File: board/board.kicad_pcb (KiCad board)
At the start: 2 copper layers, 92 x 75.8 mm, 69 parts, among them J2 Conn_01x01, J3 Conn_01x01, J3 Conn_01x25_Socket, J4 Conn_01x01, J4 Conn_01x25_Socket, J5 Conn_01x01, J5 PJ-320B, J6 Screw_Terminal_01x02, J7 Screw_Terminal_01x02, J8 Screw_Terminal_01x02

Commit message: add РПЗ template
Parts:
- removed H1: MountingHole, MountingHole:MountingHole_3.2mm_M3
- moved G*** 38.5 mm to (126.8, 101.4)
- moved J6 23.7 mm to (186.4, 86.2)
- moved J7 23.0 mm to (186.4, 94.5)
- moved J8 22.5 mm to (186.4, 103.0)
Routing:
- net PWM2: track 0.00 -> 51.4 mm
- net NOISE_CS: track 0.00 -> 27.4 mm, vias 0 -> 2
- net NOISE_DI: track 0.00 -> 25.4 mm
- net Analog_data: track 10.9 -> 34.7 mm
- net MUX_SEL_3: track 0.00 -> 23.6 mm
- net MUX_SEL_1: track 0.00 -> 20.9 mm
- net MUX_SEL_2: track 0.00 -> 20.7 mm
- net CS_AD9833_2: track 0.00 -> 19.2 mm
- net PWM4: track 0.00 -> 18.7 mm
- net NOISE_CLK_SEL: track 0.00 -> 18.1 mm
- net MUX_SEL_4: track 0.00 -> 16.8 mm
- net NOISE_CLK: track 0.00 -> 14.9 mm

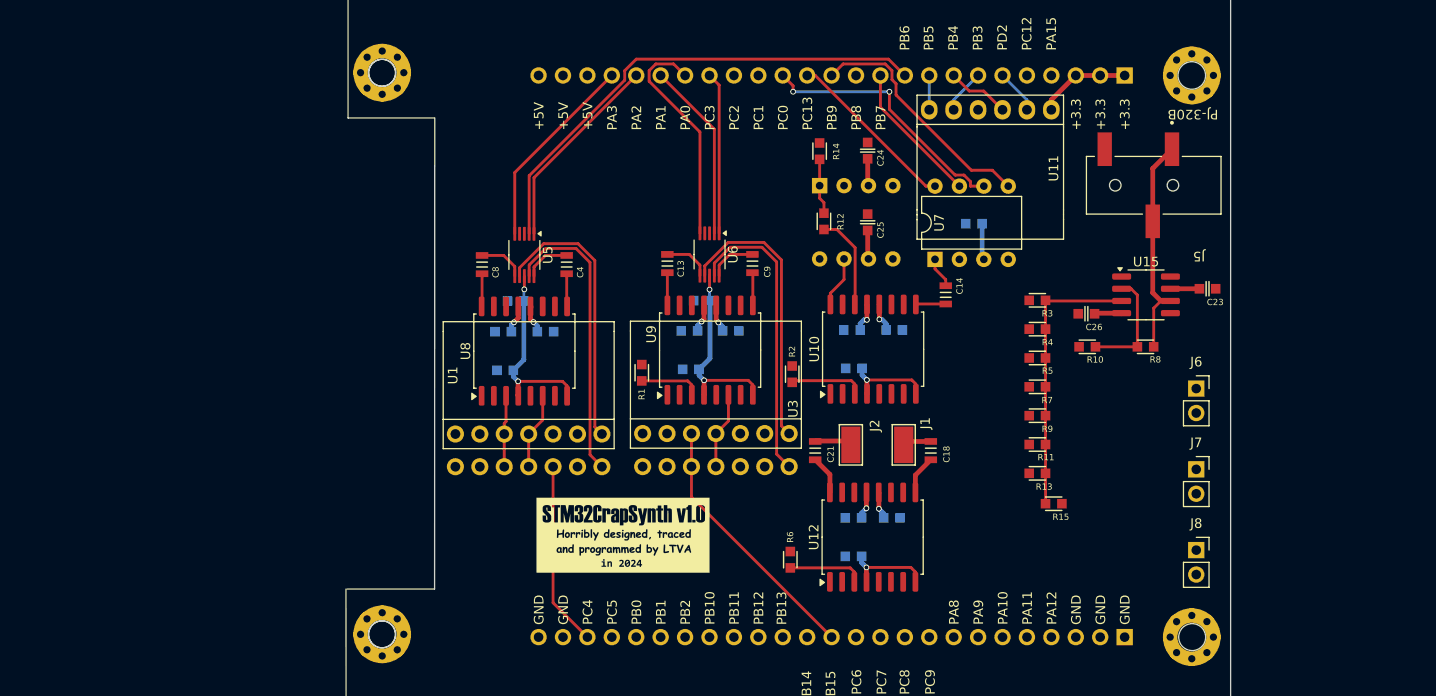
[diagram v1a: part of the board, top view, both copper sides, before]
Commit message: added DMA init
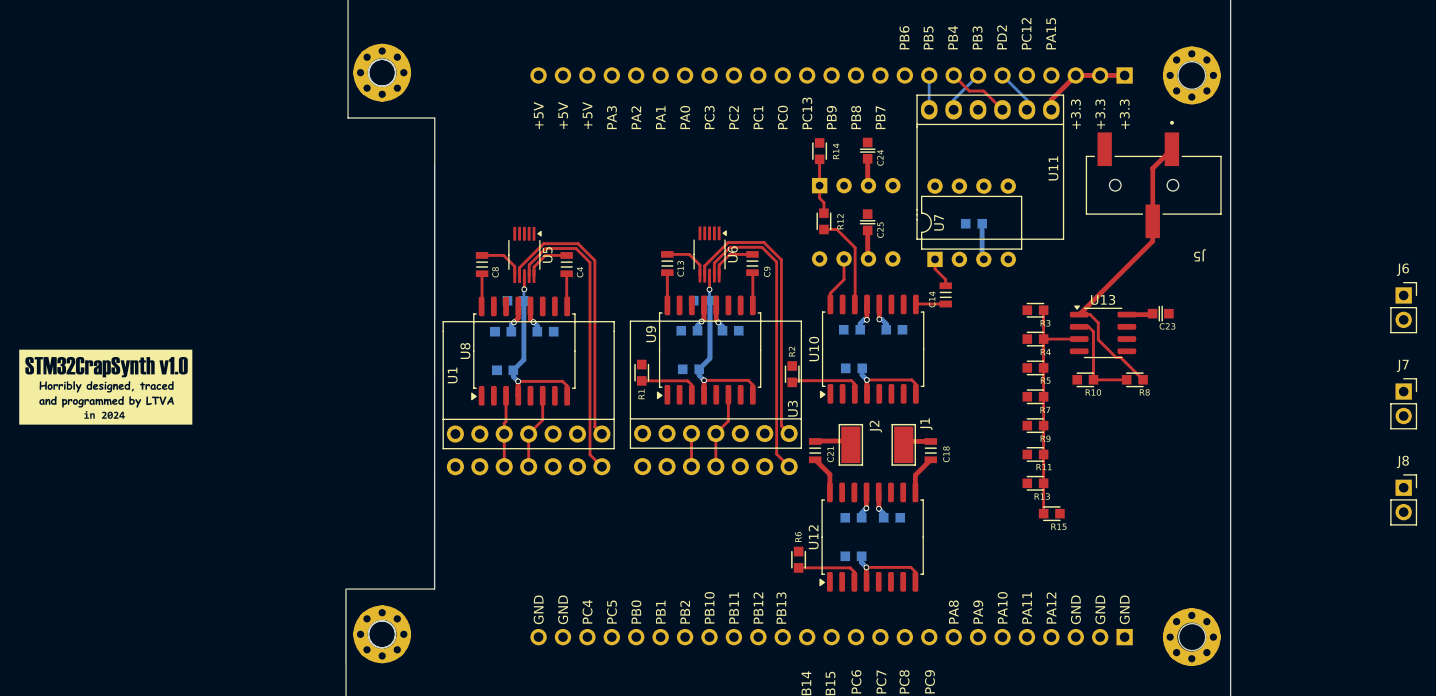
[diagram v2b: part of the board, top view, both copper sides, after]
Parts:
- removed C26: 0.22uF_0603_25V, 4ms_Capacitor:C_0603
- removed U15: ~, Package_SO:SOP-8_3.76x4.96mm_P1.27mm
- added U13: ~, Package_SO:SOIC-8_3.9x4.9mm_P1.27mm, F.Cu at (176.7, 80.4)
- moved G*** 56.0 mm to (73.0, 86.0)
- moved J6 23.7 mm to (208.0, 76.5)
- moved J7 23.0 mm to (208.0, 86.5)
- moved J8 22.5 mm to (208.0, 96.5)
- moved C23 5.52 mm to (182.7, 78.4)
- moved R8 3.61 mm to (180.0, 85.2)
- moved R10 3.44 mm to (174.9, 85.2)
- moved R11 1.05 mm to (169.7, 93.0)
- moved R13 1.05 mm to (169.7, 96.0)
- moved R3 1.05 mm to (169.7, 78.0)
- moved R4 1.05 mm to (169.7, 81.0)
- moved R5 1.05 mm to (169.7, 84.0)
- moved R7 1.05 mm to (169.7, 87.0)
- moved R9 1.05 mm to (169.7, 90.0)
- moved R15 1.05 mm to (171.4, 99.2)
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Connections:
- C23 pad 1: P,+15 -> +5V
- J3 pad 11: /PC7 -> ZCEN_2
- J3 pad 12: ATTEN_CS -> ZCEN_1
- J3 pad 14: ZCEN_DAC -> /PB14/adc4_in4
- J3 pad 16: ZCEN_2 -> /PB12/adc4_in3
- J3 pad 17: CS_AD9833_4 -> /PB11
- J3 pad 18: CS_AD9833_3 -> /PB10
- J3 pad 19: ZCEN_1 -> /PB2
- J3 pad 22: CS_AD9833_1 -> /PC5/adc2_in11
- J3 pad 23: CS_AD9833_2 -> /PC4/adc2_in5
- J3 pad 6: /PA10 -> CS_AD9833_3
- J3 pad 7: /PA9 -> CS_AD9833_2
- J3 pad 9: /PC9 -> ZCEN_DAC
- J4 pad 14: NOISE_CLK_SEL -> MUX_SEL_3
- J4 pad 15: NOISE_CS -> MUX_SEL_4
- J4 pad 16: /PC1 -> NOISE_CLK_SEL
- J4 pad 18: MUX_SEL_4 -> MUX_SEL_1
- J4 pad 19: MUX_SEL_3 -> MUX_SEL_2
- J4 pad 21: MUX_SEL_1 -> ATTEN_CS
- J4 pad 22: MUX_SEL_2 -> CS_AD9833_1
- J4 pad 4: /PA15 -> NOISE_CS
- J4 pad 5: /PC12 -> CS_AD9833_4
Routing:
- net PWM2: track 51.4 -> 0.00 mm
- net NOISE_CS: track 27.4 -> 0.00 mm, vias 2 -> 0
- net NOISE_DI: track 25.4 -> 0.00 mm
- net Analog_data: track 34.7 -> 10.9 mm
- net MUX_SEL_3: track 23.6 -> 0.00 mm
- net MUX_SEL_1: track 20.9 -> 0.00 mm
- net MUX_SEL_2: track 20.7 -> 0.00 mm
- net CS_AD9833_2: track 19.2 -> 0.00 mm
- net PWM4: track 18.7 -> 0.00 mm
- net NOISE_CLK_SEL: track 18.1 -> 0.00 mm
- net MUX_SEL_4: track 16.8 -> 0.00 mm
- net NOISE_CLK: track 14.9 -> 0.00 mm
- net Net-(U13-OUT_A): track 23.0 -> 31.7 mm
- net Net-(U13-IN_A): track 29.1 -> 24.9 mm
- net P,+15: track 14.9 -> 11.9 mm
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
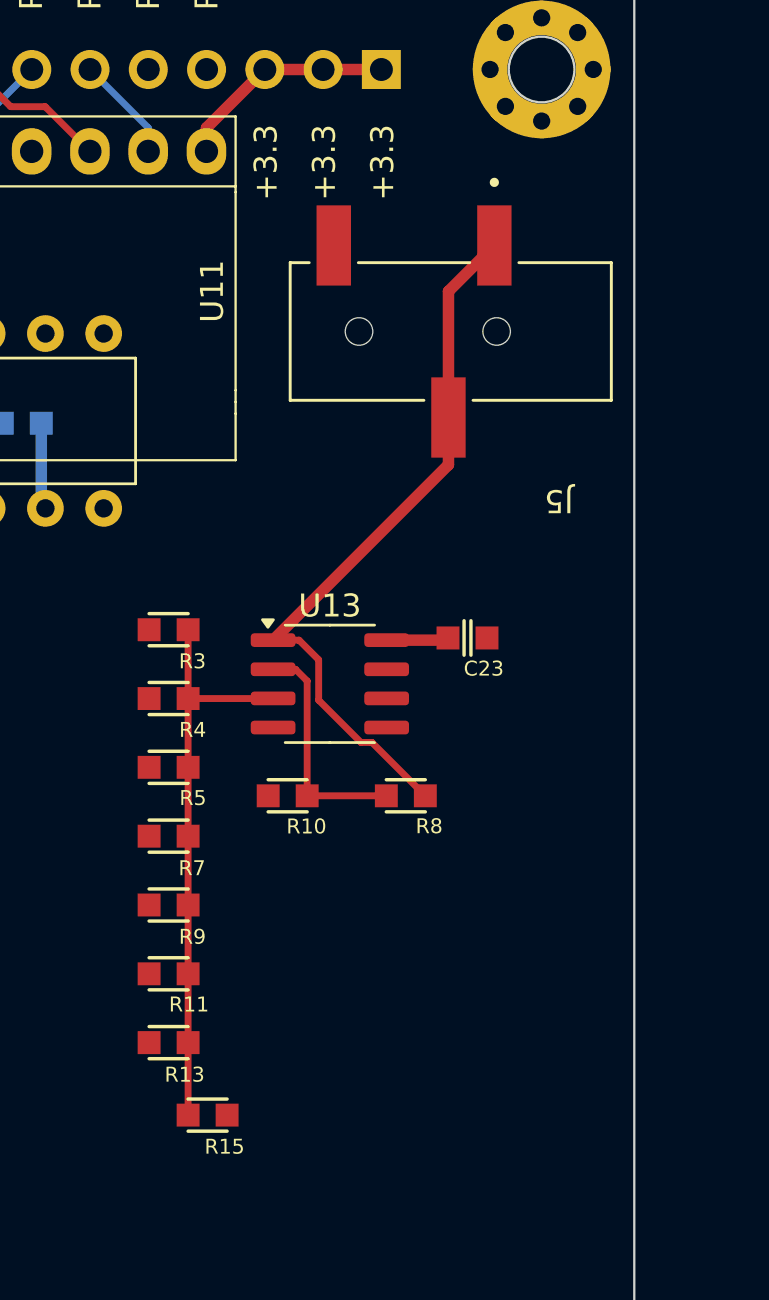
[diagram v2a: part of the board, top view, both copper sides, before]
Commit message: new opamp, timers init
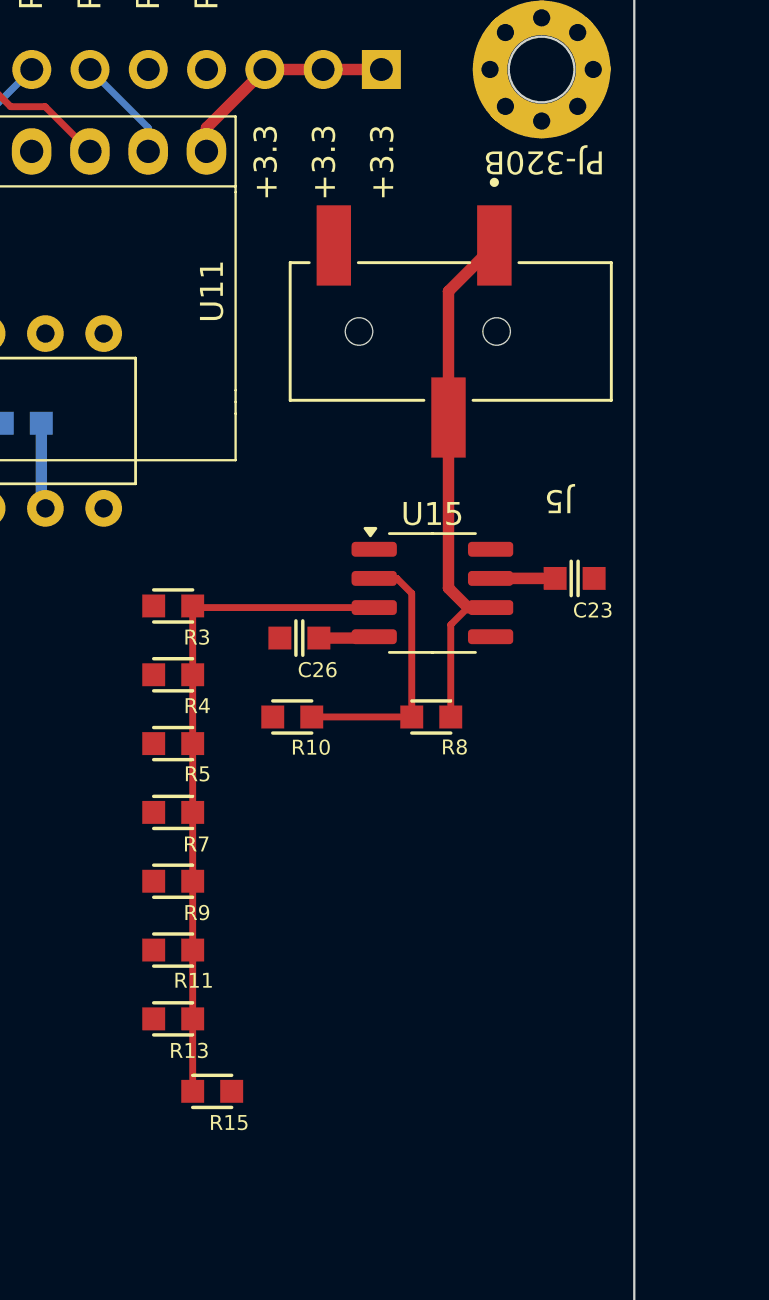
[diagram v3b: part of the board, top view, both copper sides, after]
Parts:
- removed U13: ~, Package_SO:SOIC-8_3.9x4.9mm_P1.27mm
- added C26: 0.22uF_0603_25V, 4ms_Capacitor:C_0603, F.Cu at (175.4, 78.4)
- added U15: ~, Package_SO:SOP-8_3.76x4.96mm_P1.27mm, F.Cu at (181.2, 76.4)
- moved C23 5.34 mm to (187.4, 75.8)
- moved R8 3.61 mm to (181.2, 81.8)
- moved R10 3.44 mm to (175.1, 81.8)
- moved R11 1.05 mm to (169.9, 92.0)
- moved R13 1.05 mm to (169.9, 95.0)
- moved R3 1.05 mm to (169.9, 77.0)
- moved R4 1.05 mm to (169.9, 80.0)
- moved R5 1.05 mm to (169.9, 83.0)
- moved R7 1.05 mm to (169.9, 86.0)
- moved R9 1.05 mm to (169.9, 89.0)
- moved R15 1.05 mm to (171.6, 98.1)
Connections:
- C23 pad 1: +5V -> P,+15
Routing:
- net Net-(U15-Out): track 31.7 -> 23.0 mm
- net Net-(U15-In+): track 24.9 -> 29.1 mm
- net P,+15: track 11.9 -> 14.7 mm
- net +5V: track 66.8 -> 64.1 mm
- net P,-15: track 11.9 -> 14.3 mm
- net Net-(U15-In-): track 10.2 -> 11.7 mm

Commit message: more board rework, UART & SPI init
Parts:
- added H1: MountingHole, MountingHole:MountingHole_3.2mm_M3, F.Cu at (3.48, 3.48)
- moved G*** 19.0 mm to (92.0, 84.9)
- moved R6 0.87 mm to (144.2, 104.0)
- moved C26 0.40 mm to (175.0, 78.4)
- moved C23 0.20 mm to (187.6, 75.8)
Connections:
- J3 pad 11: ZCEN_2 -> /PC7
- J3 pad 12: ZCEN_1 -> ATTEN_CS
- J3 pad 14: /PB14/adc4_in4 -> ZCEN_DAC
- J3 pad 16: /PB12/adc4_in3 -> ZCEN_2
- J3 pad 17: /PB11 -> CS_AD9833_4
- J3 pad 18: /PB10 -> CS_AD9833_3
- J3 pad 19: /PB2 -> ZCEN_1
- J3 pad 22: /PC5/adc2_in11 -> CS_AD9833_1
- J3 pad 23: /PC4/adc2_in5 -> CS_AD9833_2
- J3 pad 6: CS_AD9833_3 -> /PA10
- J3 pad 7: CS_AD9833_2 -> /PA9
- J3 pad 9: ZCEN_DAC -> /PC9
- J4 pad 14: MUX_SEL_3 -> NOISE_CLK_SEL
- J4 pad 15: MUX_SEL_4 -> NOISE_CS
- J4 pad 16: NOISE_CLK_SEL -> /PC1
- J4 pad 18: MUX_SEL_1 -> MUX_SEL_4
- J4 pad 19: MUX_SEL_2 -> MUX_SEL_3
- J4 pad 21: ATTEN_CS -> MUX_SEL_1
- J4 pad 22: CS_AD9833_1 -> MUX_SEL_2
- J4 pad 4: NOISE_CS -> /PA15
- J4 pad 5: CS_AD9833_4 -> /PC12
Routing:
- net Analog_data_out3: track 7.00 -> 7.86 mm
